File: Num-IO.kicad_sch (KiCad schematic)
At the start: 15 parts, among them U3 MAX14851AEE+

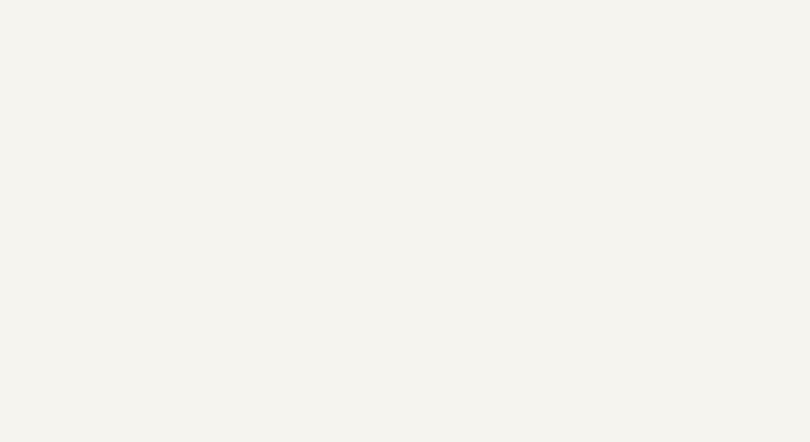
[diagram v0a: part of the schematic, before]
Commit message: add KK connectors for power (check voltage or bypass)
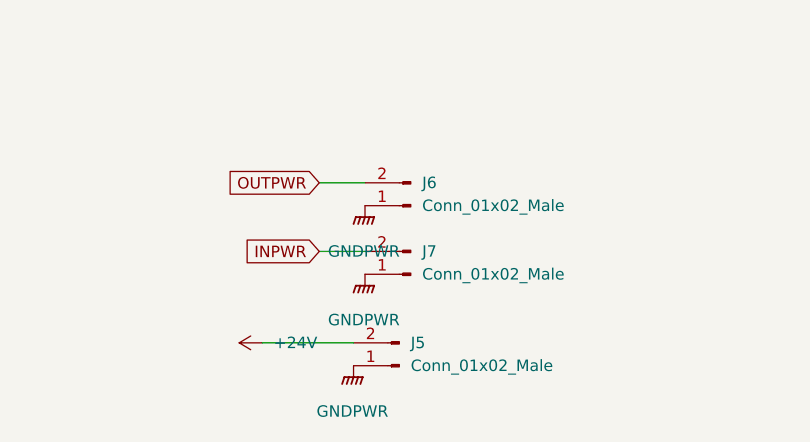
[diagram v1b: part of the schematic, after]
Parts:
- added J5, J6, J7: Conn_01x02_Male, Connector_Molex:Molex_KK-254_AE-6410-02A_1x02_P2.54mm_Vertical, symbol Connector:Conn_01x02_Male
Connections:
- net +24V: now also J5.2 (Pin_2)
- net GNDPWR: now also J5.1 (Pin_1), J6.1 (Pin_1), J7.1 (Pin_1)
- net INPWR: now also J7.2 (Pin_2)
- net OUTPWR: now also J6.2 (Pin_2)

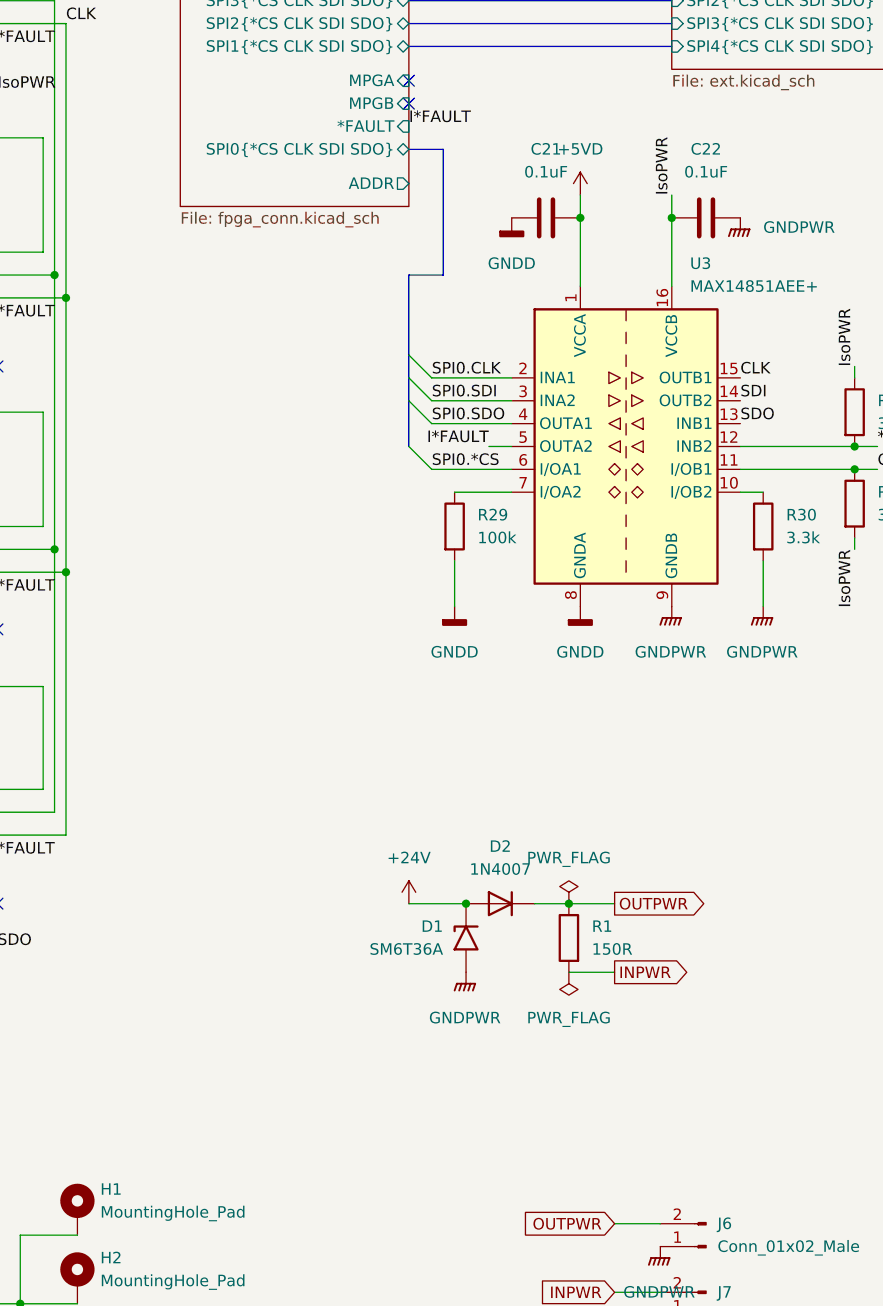
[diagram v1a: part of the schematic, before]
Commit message: add resistances for bypassing the isolator
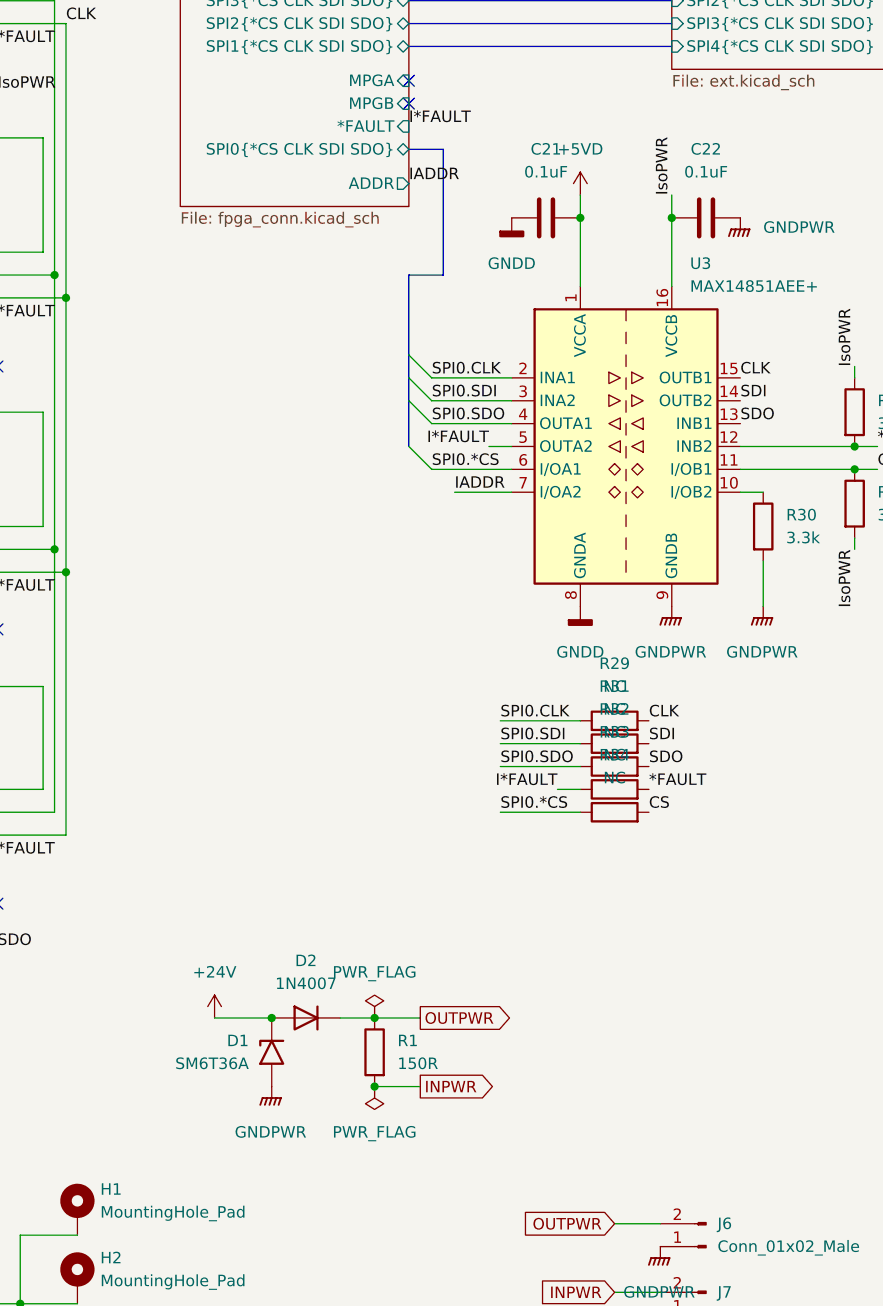
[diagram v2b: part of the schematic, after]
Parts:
- added R31, R32, R33, R34: NC, Resistor_SMD:R_0805_2012Metric_Pad1.20x1.40mm_HandSolder, symbol Device:R
- R29: value 100k -> NC; footprint Resistor_SMD:R_0603_1608Metric -> Resistor_SMD:R_0805_2012Metric_Pad1.20x1.40mm_HandSolder
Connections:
- net *FAULT: now also R33.2
- net CLK: now also R29.2
- net CS: now also R34.2
- net GNDD: no longer R29.2
- net I*FAULT: now also R33.1
- net SDI: now also R31.2
- net SDO: now also R32.2
- net SPI0.*CS: now also R34.1
- net SPI0.CLK: now also R29.1
- net SPI0.SDI: now also R31.1
- net SPI0.SDO: now also R32.1
- net IADDR: now reaches U3.7 (I/OA2)
- net IADDR: no longer R29.1
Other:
- moved on the sheet: D1, D2, R1

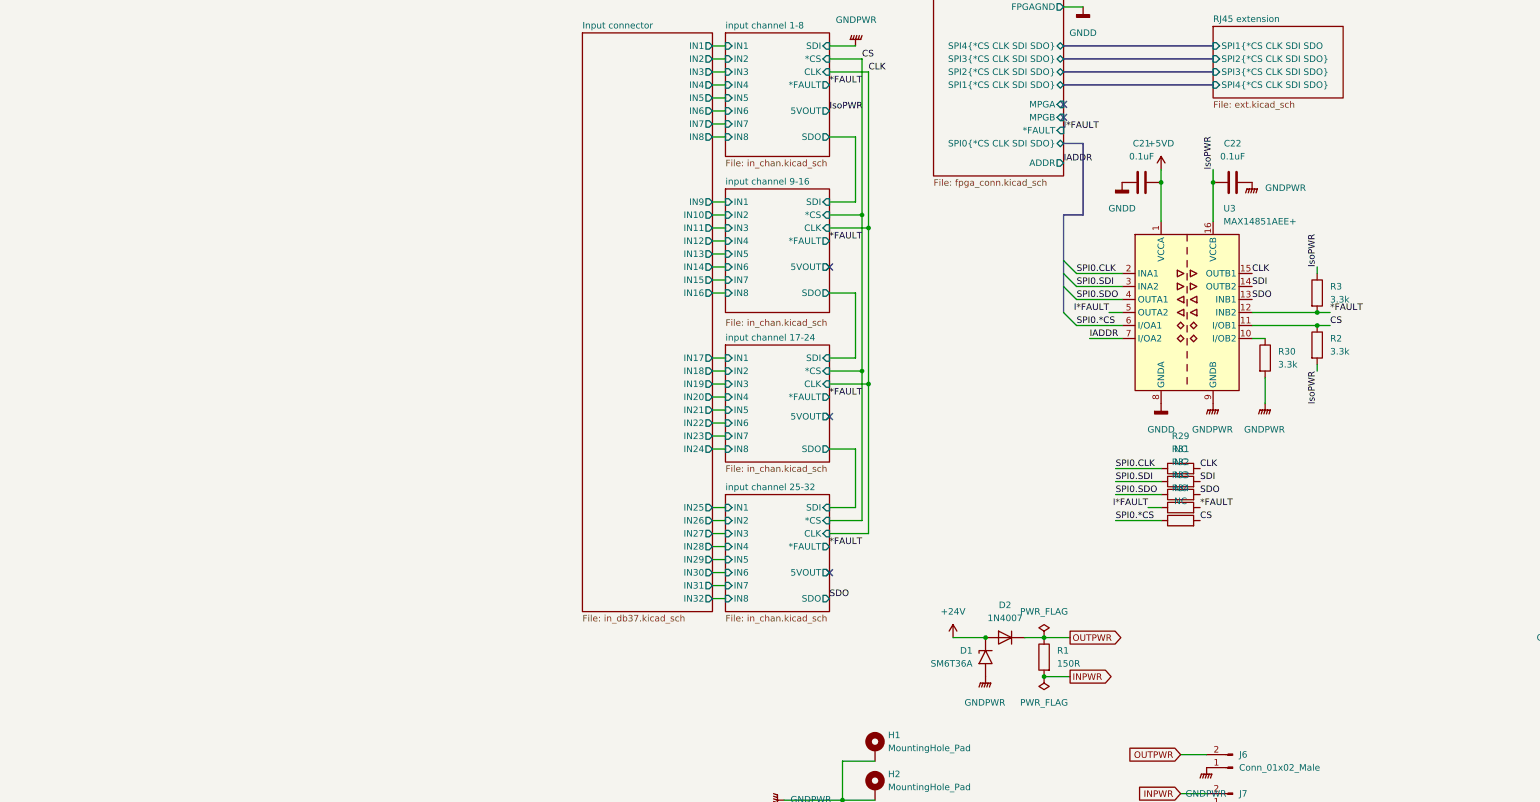
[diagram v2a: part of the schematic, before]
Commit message: add MPGA and MPGB on a DB25 (isolated)
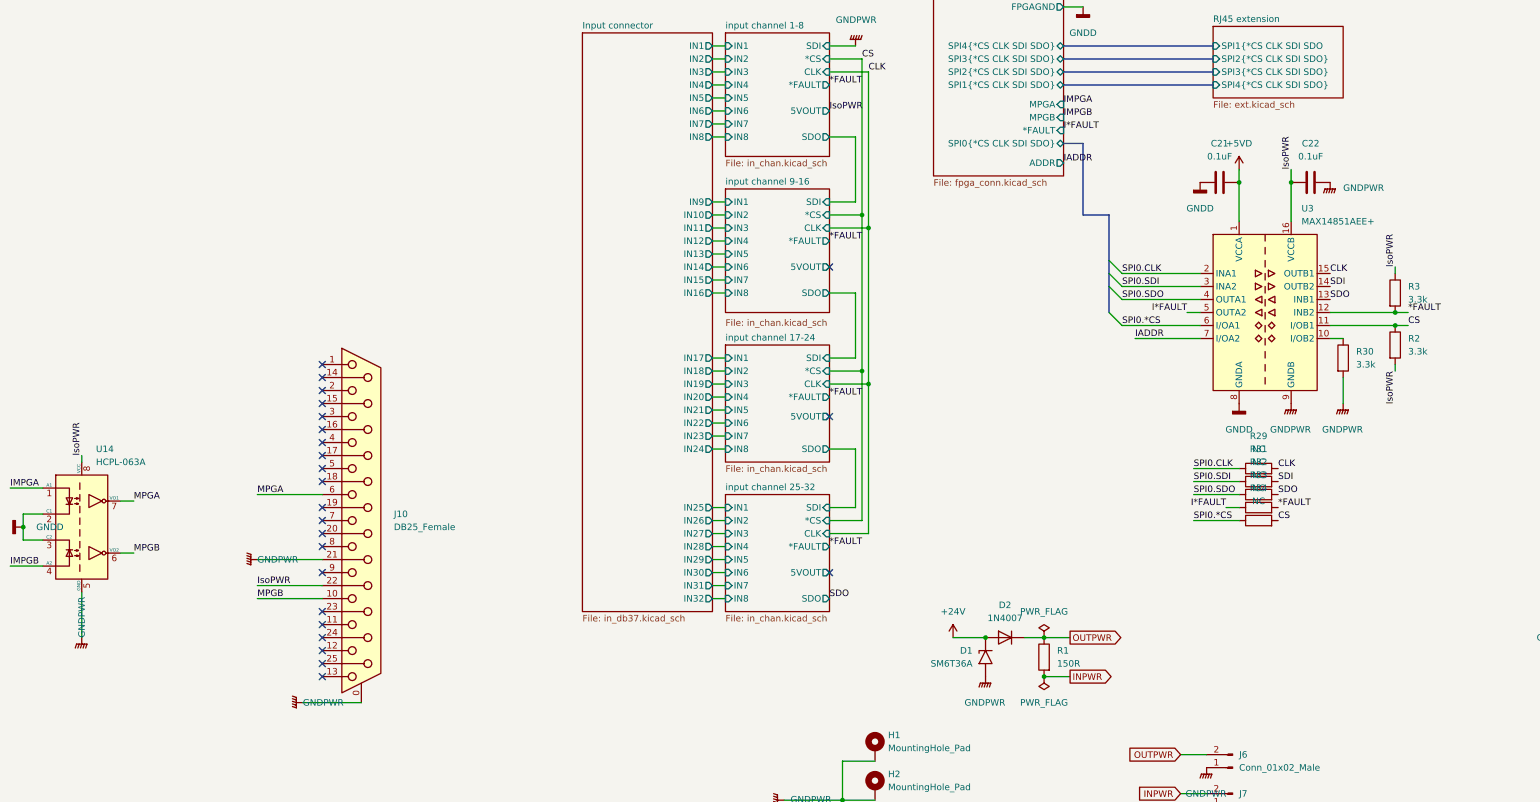
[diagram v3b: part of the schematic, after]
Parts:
- added J10: DB25_Female, Connector_Dsub:DSUB-25_Female_Vertical_P2.77x2.84mm_MountingHoles, symbol Connector:DB25_Female_MountingHoles
- added U14: HCPL-063A, Package_SO:SOIC-8_3.9x4.9mm_P1.27mm, symbol Isolator:HCPL-063A
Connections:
- net GNDD: now also U14.2 (C1), U14.3 (C2)
- net GNDPWR: now also J10.0 (PAD), J10.21 (P21), U14.5 (GND)
- net IsoPWR: now also J10.22 (P22), U14.8 (VCC)
- new net IMPGA: U14.1 (A1)
- new net IMPGB: U14.4 (A2)
- new net MPGA: J10.6, U14.7 (VO1)
- new net MPGB: J10.10, U14.6 (VO2)
- no-connect marks 8 -> 27
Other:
- moved on the sheet: C21, C22, R2, R29, R3, R30, R31, R32, R33, R34, U3

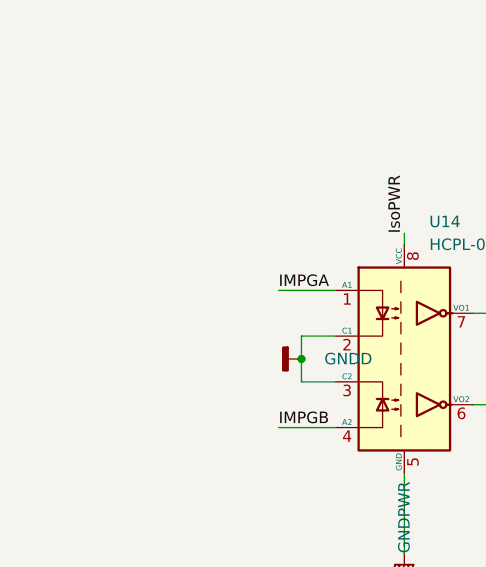
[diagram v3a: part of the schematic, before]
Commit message: add condo for MPG isolator + small rerouting pair diff
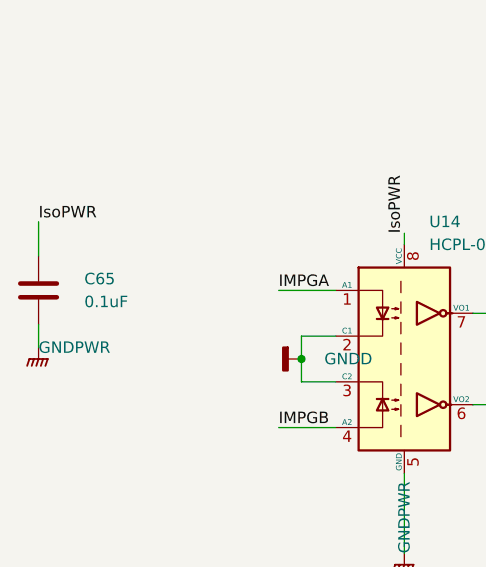
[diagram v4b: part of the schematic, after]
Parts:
- added C65: 0.1uF, Capacitor_SMD:C_0805_2012Metric, symbol Device:C
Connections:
- net GNDPWR: now also C65.1
- net IsoPWR: now also C65.2
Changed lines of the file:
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@@
+    (stroke (width 0) (type default) (color 0 0 0 0))
+  )
+  (wire (pts (xy -120.65 109.22) (xy -120.65 113.03))
     (stroke (width 0) (type default) (color 0 0 0 0))
   )
@@
   )
   (wire (pts (xy 43.18 93.98) (xy 45.72 93.98))
+    (stroke (width 0) (type default) (color 0 0 0 0))
+  )
+  (wire (pts (xy -120.65 123.19) (xy -120.65 120.65))
     (stroke (width 0) (type default) (color 0 0 0 0))
   )
@@
   )
   (label "CS" (at 153.67 123.19 0)
+    (effects (font (size 1.27 1.27)) (justify left bottom))
+  )
+  (label "IsoPWR" (at -120.65 109.22 0)
     (effects (font (size 1.27 1.27)) (justify left bottom))
   )
@@
     (pin "2")
   )
+  (symbol (lib_id "Device:C") (at -120.65 116.84 180) (unit 1)
+    (in_bom yes) (on_board yes) (fields_autoplaced)
+    (property "Reference" "C65" (id 0) (at -115.57 115.5699 0)
+      (effects (font (size 1.27 1.27)) (justify right))
+    )
+    (property "Value" "0.1uF" (id 1) (at -115.57 118.1099 0)
+      (effects (font (size 1.27 1.27)) (justify right))
+    )
+    (property "Footprint" "Capacitor_SMD:C_0805_2012Metric" (id 2) (at -121.6152 113.03 0)
+      (effects (font (size 1.27 1.27)) hide)
+    )
+    (property "Datasheet" "~" (id 3) (at -120.65 116.84 0)
+      (effects (font (size 1.27 1.27)) hide)
+    )
+    (pin "1")
+    (pin "2")
+  )
   (symbol (lib_id "Diode:SM4007") (at 100.33 146.05 0) (mirror y) (unit 1)
     (in_bom yes) (on_board yes) (fields_autoplaced)
@@
     )
     (property "Datasheet" "~" (id 3) (at 107.95 153.67 0)
+      (effects (font (size 1.27 1.27)) hide)
+    )
+    (pin "1")
+  )
+  (symbol (lib_id "power:GNDPWR") (at -120.65 123.19 0) (unit 1)
+    (in_bom yes) (on_board yes)
+    (property "Reference" "#PWR075" (id 0) (at -120.65 128.27 0)
+      (effects (font (size 1.27 1.27)) hide)
+    )
+    (property "Value" "GNDPWR" (id 1) (at -120.65 123.19 0)
+      (effects (font (size 1.27 1.27)) (justify left))
+    )
+    (property "Footprint" "" (id 2) (at -120.65 124.46 0)
+      (effects (font (size 1.27 1.27)) hide)
+    )
+    (property "Datasheet" "" (id 3) (at -120.65 124.46 0)
       (effects (font (size 1.27 1.27)) hide)
     )
@@
       (reference "#PWR074") (unit 1) (value "GNDD") (footprint "")
     )
+    (path "/2896db9d-bbd4-47f7-9b1a-06d1f965562f"
+      (reference "#PWR075") (unit 1) (value "GNDPWR") (footprint "")
+    )
     (path "/1d55f859-b955-4956-adf8-4e32f584531b/44640c58-6ca2-41bc-97df-f34b590da73d"
       (reference "#PWR083") (unit 1) (value "GNDD") (footprint "")
@@
       (reference "C64") (unit 1) (value "<27pF") (footprint "Capacitor_SMD:C_0603_1608Metric")
     )
+    (path "/1f6c03aa-8cb1-466f-97e6-453330aad65f"
+      (reference "C65") (unit 1) (value "0.1uF") (footprint "Capacitor_SMD:C_0805_2012Metric")
+    )
     (path "/c822509d-e9f4-4efb-ba8f-114860c2cd02"
